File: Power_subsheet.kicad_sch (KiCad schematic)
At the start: 26 parts, among them U5 LM1117MP-ADJ, U7 TPS54331-Q1

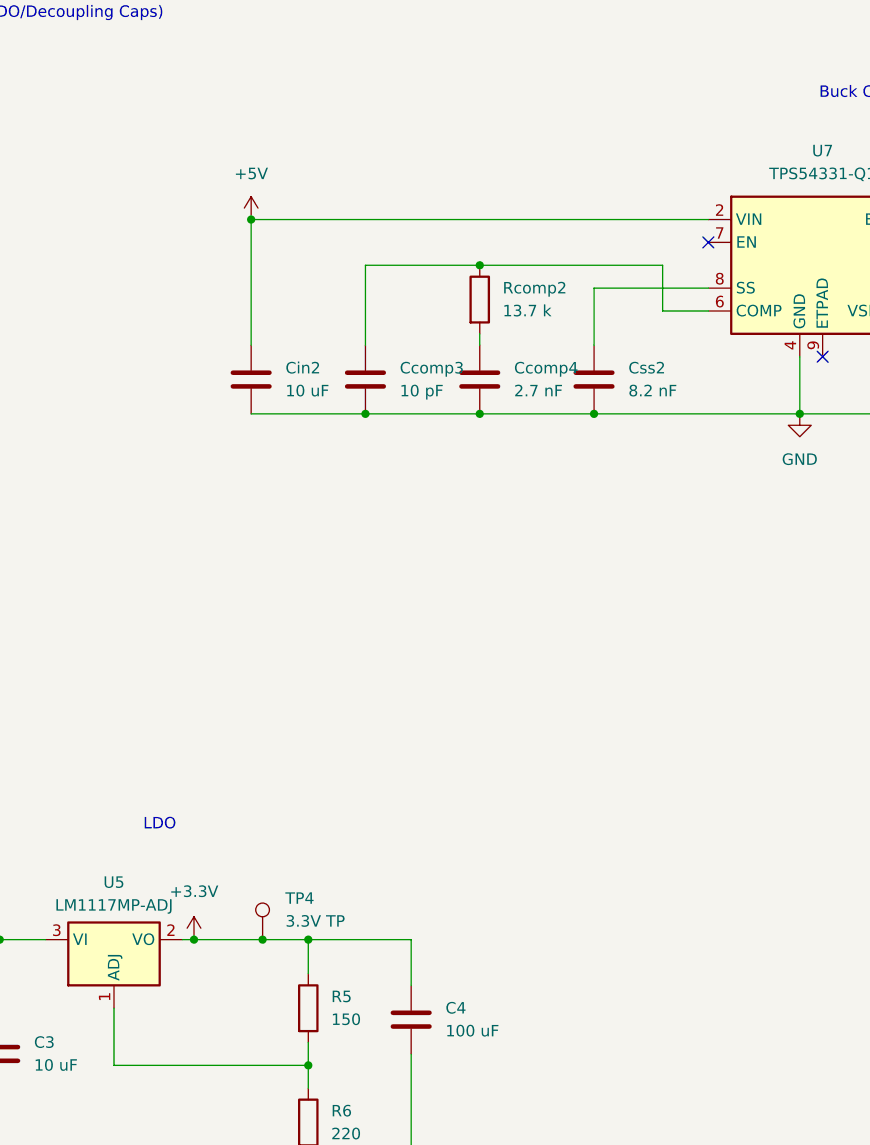
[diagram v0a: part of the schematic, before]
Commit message: remove un-needed program header circuitry, add debug LEDs, add USB ESD, add shcotty for LM117
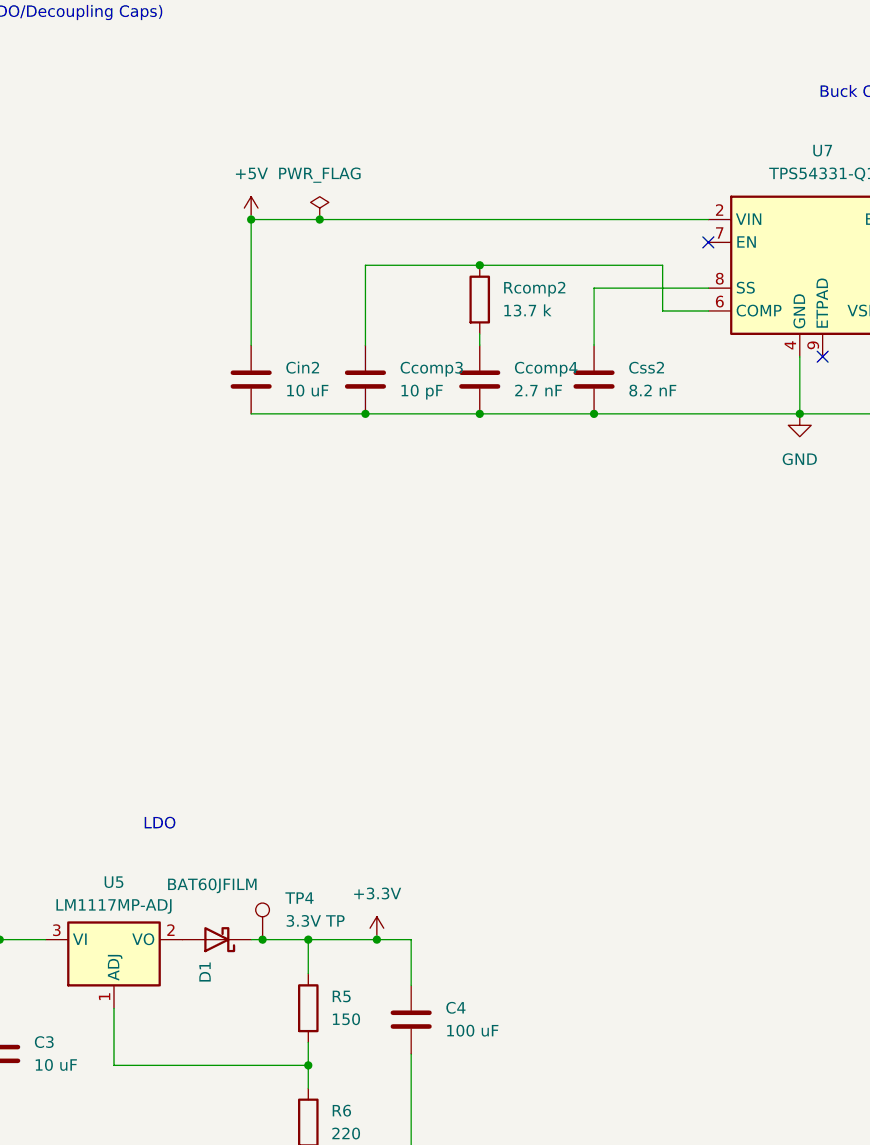
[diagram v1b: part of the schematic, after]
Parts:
- added D1: BAT60JFILM, Diode_SMD:D_0805_2012Metric_Pad1.15x1.40mm_HandSolder, symbol Device:D_Schottky
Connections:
- net +3.3V: now also D1.1 (K); no longer U5.2 (VO)
- new net: D1.2 (A), U5.2 (VO)

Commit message: more cap changes
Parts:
- added C6: 4.7 uF, Capacitor_SMD:C_0805_2012Metric_Pad1.18x1.45mm_HandSolder, symbol Device:C
- added C7: 1 uF, Capacitor_SMD:C_0805_2012Metric_Pad1.18x1.45mm_HandSolder, symbol Device:C
- C21: value 10 uF -> 10 nF
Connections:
- net +3.3V: now also C6.1, C7.1
- net GND: now also C6.2, C7.2
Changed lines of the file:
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@@
 	)
 	(junction
+		(at 242.57 133.35)
+		(diameter 0)
+		(color 0 0 0 0)
+	)
+	(junction
 		(at 220.98 140.97)
 		(diameter 0)
@@
 	)
 	(junction
+		(at 255.27 133.35)
+		(diameter 0)
+		(color 0 0 0 0)
+	)
+	(junction
 		(at 134.62 67.31)
 		(diameter 0)
@@
 	)
 	(junction
+		(at 255.27 140.97)
+		(diameter 0)
+		(color 0 0 0 0)
+	)
+	(junction
 		(at 210.82 140.97)
 		(diameter 0)
@@
 	(wire
 		(pts
+			(xy 242.57 133.35) (xy 255.27 133.35)
+		)
+		(stroke
+			(width 0)
+			(type default)
+		)
+	)
+	(wire
+		(pts
 			(xy 99.06 58.42) (xy 99.06 59.69)
 		)
@@
 	(wire
 		(pts
+			(xy 255.27 133.35) (xy 267.97 133.35)
+		)
+		(stroke
+			(width 0)
+			(type default)
+		)
+	)
+	(wire
+		(pts
 			(xy 99.06 50.8) (xy 119.38 50.8)
 		)
@@
 	(wire
 		(pts
+			(xy 242.57 140.97) (xy 255.27 140.97)
+		)
+		(stroke
+			(width 0)
+			(type default)
+		)
+	)
+	(wire
+		(pts
 			(xy 80.01 137.16) (xy 80.01 139.7)
 		)
@@
 	(wire
 		(pts
+			(xy 255.27 140.97) (xy 267.97 140.97)
+		)
+		(stroke
+			(width 0)
+			(type default)
+		)
+	)
+	(wire
+		(pts
 			(xy 220.98 133.35) (xy 231.14 133.35)
 		)
@@
 			)
 		)
-		(property "Value" "10 uF"
+		(property "Value" "10 nF"
 			(at 246.38 138.4299 0)
 			(effects
@@
 	)
 	(symbol
+		(lib_id "Device:C")
+		(at 267.97 137.16 0)
+		(unit 1)
+		(exclude_from_sim no)
+		(in_bom yes)
+		(on_board yes)
+		(dnp no)
+		(fields_autoplaced yes)
+		(property "Reference" "C7"
+			(at 271.78 135.8899 0)
+			(effects
+				(font
+					(size 1.27 1.27)
+				)
+				(justify left)
+			)
+		)
+		(property "Value" "1 uF"
+			(at 271.78 138.4299 0)
+			(effects
+				(font
+					(size 1.27 1.27)
+				)
+				(justify left)
+			)
+		)
+		(property "Footprint" "Capacitor_SMD:C_0805_2012Metric_Pad1.18x1.45mm_HandSolder"
+			(at 268.9352 140.97 0)
+			(effects
+				(font
+					(size 1.27 1.27)
+				)
+				(hide yes)
+			)
+		)
+		(property "Datasheet" "~"
+			(at 267.97 137.16 0)
+			(effects
+				(font
+					(size 1.27 1.27)
+				)
+				(hide yes)
+			)
+		)
+		(property "Description" "Unpolarized capacitor"
+			(at 267.97 137.16 0)
+			(effects
+				(font
+					(size 1.27 1.27)
+				)
+				(hide yes)
+			)
+		)
+		(pin "1"
+		)
+		(pin "2"
+		)
+		(instances
+			(project "PCB_Schematic"
+				(path "/a0c17764-e0d1-4df5-b871-1489cf266494/e6fb26c7-dfd6-4c6c-883e-94dceb19958a"
+					(reference "C7")
+					(unit 1)
+				)
+			)
+		)
+	)
+	(symbol
 		(lib_id "Device:R")
 		(at 99.06 54.61 0)
@@
 					(unit 1)
 				)
+			)
+		)
+	)
+	(symbol
+		(lib_id "Device:C")
+		(at 255.27 137.16 0)
+		(unit 1)
+		(exclude_from_sim no)
+		(in_bom yes)
+		(on_board yes)
+		(dnp no)
+		(fields_autoplaced yes)
+		(property "Reference" "C6"
+			(at 259.08 135.8899 0)
+			(effects
+				(font
+					(size 1.27 1.27)
+				)
+				(justify left)
+			)
+		)
+		(property "Value" "4.7 uF"
+			(at 259.08 138.4299 0)
+			(effects
+				(font
+					(size 1.27 1.27)
+				)
+				(justify left)
+			)
+		)
+		(property "Footprint" "Capacitor_SMD:C_0805_2012Metric_Pad1.18x1.45mm_HandSolder"
+			(at 256.2352 140.97 0)
+			(effects
+				(font
+					(size 1.27 1.27)
+				)
+				(hide yes)
+			)
+		)
+		(property "Datasheet" "~"
+			(at 255.27 137.16 0)
+			(effects
+				(font
+					(size 1.27 1.27)
+				)
+				(hide yes)
+			)
+		)
+		(property "Description" "Unpolarized capacitor"
+			(at 255.27 137.16 0)
+			(effects
+				(font
+					(size 1.27 1.27)
+				)
+				(hide yes)
+			)
+		)
+		(pin "1"
+		)
+		(pin "2"
+		)
+		(instances
+			(project "PCB_Schematic"
+				(path "/a0c17764-e0d1-4df5-b871-1489cf266494/e6fb26c7-dfd6-4c6c-883e-94dceb19958a"
+					(reference "C6")
+					(unit 1)
+				)

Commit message: starter PCB
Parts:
- C4: renamed from C3; footprint (none) -> Capacitor_SMD:C_0805_2012Metric_Pad1.18x1.45mm_HandSolder
- C5: renamed from C4; footprint (none) -> Capacitor_SMD:C_0805_2012Metric_Pad1.18x1.45mm_HandSolder
- renumbered C20 to C10, C21 to C11, C6 to C12, C7 to C13, C5 to C6, C17 to C7, C18 to C8, C19 to C9, Cboot2 to Cboot1, Ccomp3 to Ccomp1, Ccomp4 to Ccomp2, Cin2 to Cin1, Cout2 to Cout1, Css2 to Css1, D1 to D11, D2 to D12, D3 to D13, L2 to L1, R5 to R12, R6 to R13, R16 to R14, Rcomp2 to Rcomp1, Rfbb2 to Rfbb1, Rfbt2 to Rfbt1, TP4 to TP1, U5 to U3, U7 to U4

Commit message: more
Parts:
- removed U4: TPS54331-Q1, Library:Project_TPS, symbol Regulator_Switching:TPS54336ADDA
- added C16: .1 uF, Capacitor_SMD:C_0805_2012Metric_Pad1.18x1.45mm_HandSolder, symbol Device:C
- added U4: TPS54331QDRQ1, Library:Project_TPS, symbol New_Library:TPS54331QDRQ1
- U3: footprint Library:Project_LM1117 -> Package_TO_SOT_SMD:SOT-23-3
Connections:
- net +3.3V: now also C16.1
- net +5V: now also U4.2 (VIN)
- net GND: now also C16.2, U4.7 (GND)
- net at Cboot1.1: now also D12.1 (K), L1.1, U4.8 (PH)
- net at Rfbb1.1, Rfbt1.2: now also U4.5 (VSENSE)
- net at Css1.1: now also U4.4 (SS)
- net at Ccomp1.1, Rcomp1.1: now also U4.6 (COMP)
- new net: Cboot1.2, U4.1 (BOOT)
- no-connect marks 2 -> 1
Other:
- moved on the sheet: C4, C5, D11, R12, R13, TP1, U3

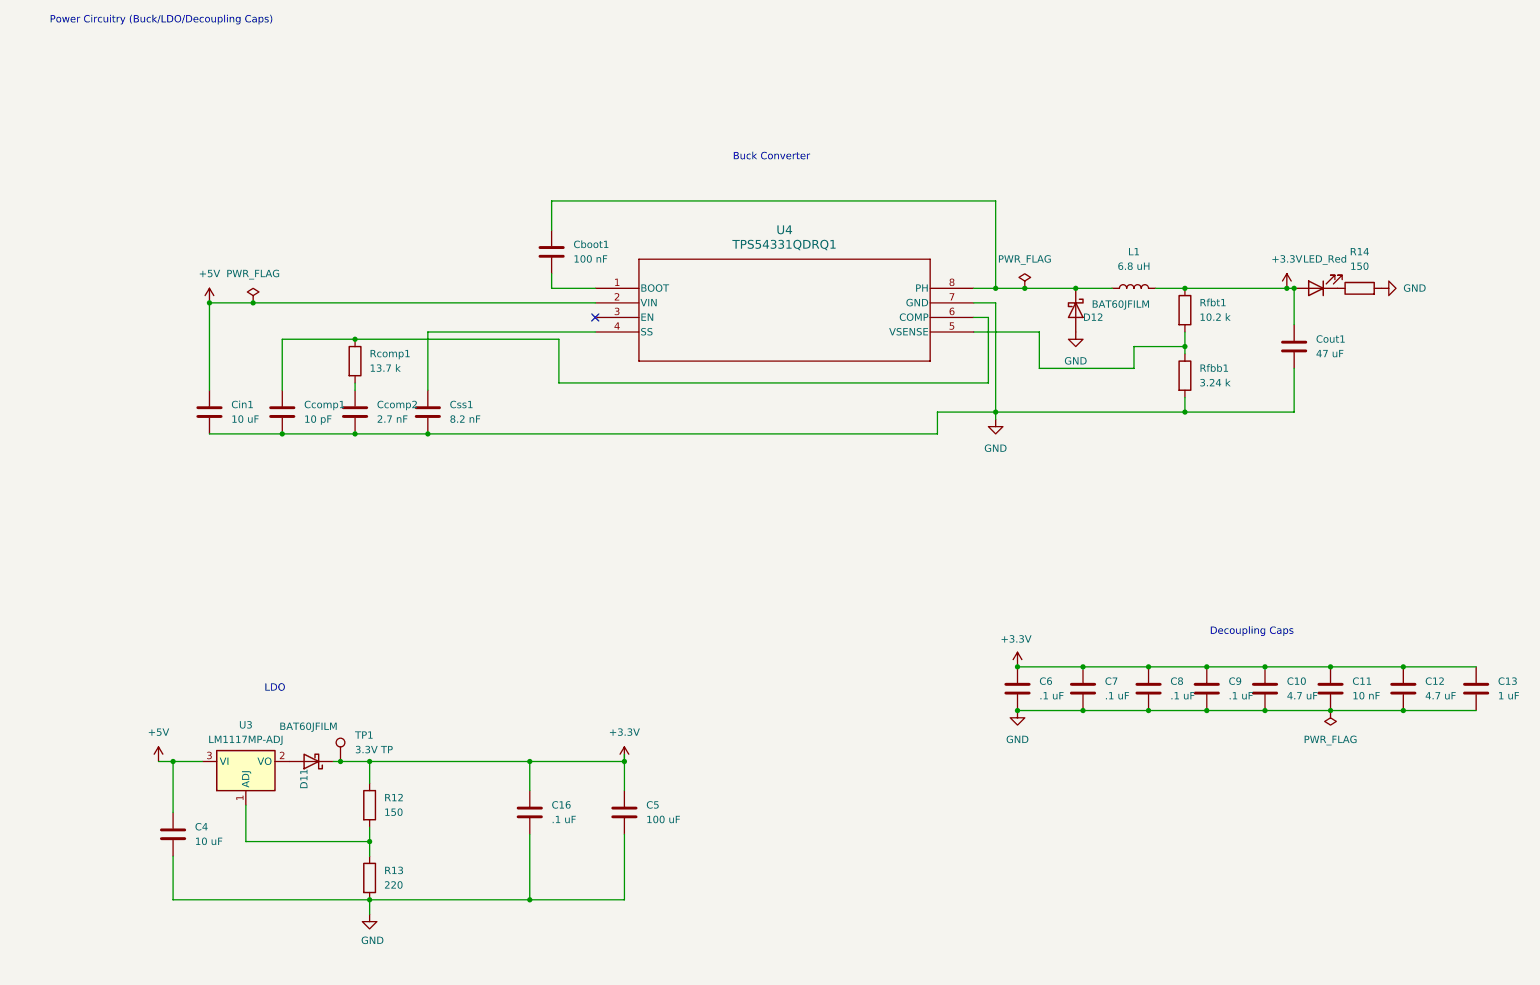
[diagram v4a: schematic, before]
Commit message: added testpoints to schematic for important sigs
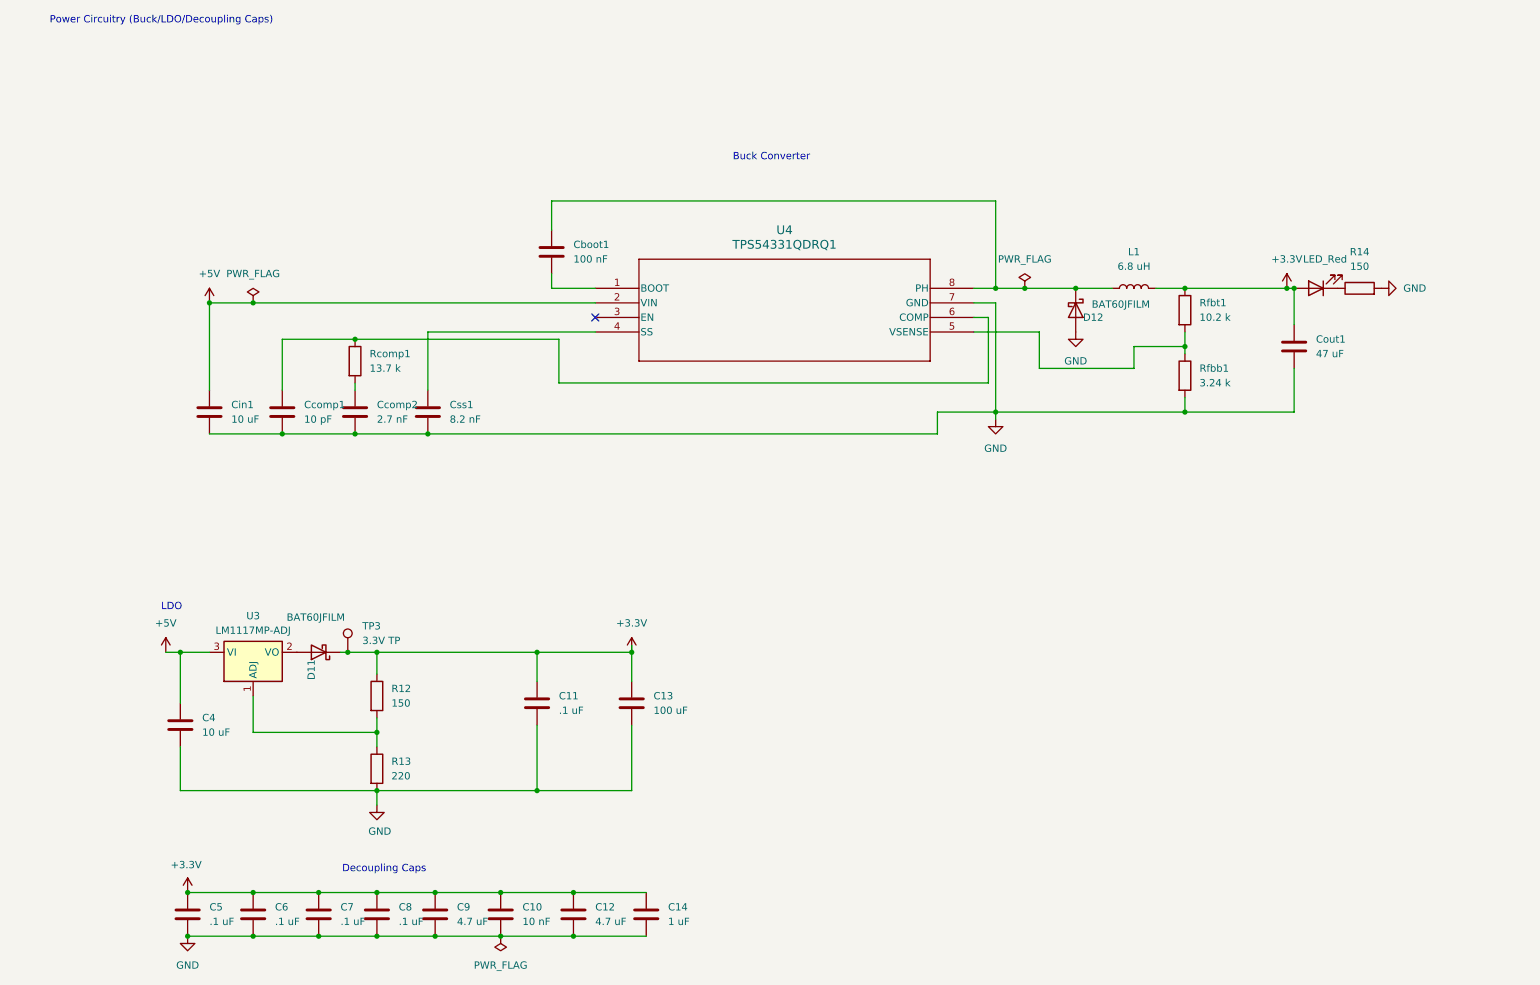
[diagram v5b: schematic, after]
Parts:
- renumbered C11 to C10, C16 to C11, C5 to C13, C13 to C14, C6 to C5, C7 to C6, C8 to C7, C9 to C8, C10 to C9, TP1 to TP3
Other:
- moved on the sheet: C10, C11, C12, C13, C14, C4, C5, C6, C7, C8, C9, D11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

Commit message: done
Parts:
- U3: footprint Package_TO_SOT_SMD:SOT-23-3 -> Library:LDO_fp
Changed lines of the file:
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@@
 			)
 		)
-		(property "Footprint" "Package_TO_SOT_SMD:SOT-23-3"
+		(property "Footprint" "Library:LDO_fp"
 			(at 54.61 130.81 0)
 			(effects

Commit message: new buck
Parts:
- Cboot1: footprint Capacitor_SMD:C_0805_2012Metric_Pad1.18x1.45mm_HandSolder -> Capacitor_SMD:C_0402_1005Metric_Pad0.74x0.62mm_HandSolder
- Cin1, Cout1: footprint Capacitor_SMD:C_0805_2012Metric_Pad1.18x1.45mm_HandSolder -> Capacitor_SMD:C_1210_3225Metric_Pad1.33x2.70mm_HandSolder
- Css1: footprint Capacitor_SMD:C_0805_2012Metric_Pad1.18x1.45mm_HandSolder -> Capacitor_SMD:C_0201_0603Metric_Pad0.64x0.40mm_HandSolder
- D12: footprint Diode_SMD:D_0805_2012Metric_Pad1.15x1.40mm_HandSolder -> Diode_SMD:D_SOD-123F
- L1: footprint Inductor_SMD:L_0805_2012Metric_Pad1.15x1.40mm_HandSolder -> Library:inductor
- Rcomp1, Rfbb1, Rfbt1: footprint Resistor_SMD:R_0805_2012Metric_Pad1.20x1.40mm_HandSolder -> Capacitor_SMD:C_0402_1005Metric_Pad0.74x0.62mm_HandSolder
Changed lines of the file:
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@@
 			)
 		)
-		(property "Footprint" "Resistor_SMD:R_0805_2012Metric_Pad1.20x1.40mm_HandSolder"
+		(property "Footprint" "Capacitor_SMD:C_0402_1005Metric_Pad0.74x0.62mm_HandSolder"
 			(at 70.612 80.01 90)
 			(effects
@@
 			)
 		)
-		(property "Footprint" "Capacitor_SMD:C_0805_2012Metric_Pad1.18x1.45mm_HandSolder"
+		(property "Footprint" "Capacitor_SMD:C_0201_0603Metric_Pad0.64x0.40mm_HandSolder"
 			(at 86.0552 92.71 0)
 			(effects
@@
 			)
 		)
-		(property "Footprint" "Resistor_SMD:R_0805_2012Metric_Pad1.20x1.40mm_HandSolder"
+		(property "Footprint" "Capacitor_SMD:C_0402_1005Metric_Pad0.74x0.62mm_HandSolder"
 			(at 215.392 82.55 90)
 			(effects
@@
 			)
 		)
-		(property "Footprint" "Capacitor_SMD:C_0805_2012Metric_Pad1.18x1.45mm_HandSolder"
+		(property "Footprint" "Capacitor_SMD:C_1210_3225Metric_Pad1.33x2.70mm_HandSolder"
 			(at 47.9552 92.71 0)
 			(effects
@@
 			)
 		)
-		(property "Footprint" "Inductor_SMD:L_0805_2012Metric_Pad1.15x1.40mm_HandSolder"
+		(property "Footprint" "Library:inductor"
 			(at 208.28 67.31 0)
 			(effects
@@
 			)
 		)
-		(property "Footprint" "Resistor_SMD:R_0805_2012Metric_Pad1.20x1.40mm_HandSolder"
+		(property "Footprint" "Capacitor_SMD:C_0402_1005Metric_Pad0.74x0.62mm_HandSolder"
 			(at 215.392 71.12 90)
 			(effects
@@
 			)
 		)
-		(property "Footprint" "Diode_SMD:D_0805_2012Metric_Pad1.15x1.40mm_HandSolder"
+		(property "Footprint" "Diode_SMD:D_SOD-123F"
 			(at 198.12 71.12 0)
 			(effects
@@
 			)
 		)
-		(property "Footprint" "Capacitor_SMD:C_0805_2012Metric_Pad1.18x1.45mm_HandSolder"
+		(property "Footprint" "Capacitor_SMD:C_1210_3225Metric_Pad1.33x2.70mm_HandSolder"
 			(at 237.1852 81.28 0)
 			(effects
@@
 			)
 		)
-		(property "Footprint" "Capacitor_SMD:C_0805_2012Metric_Pad1.18x1.45mm_HandSolder"
+		(property "Footprint" "Capacitor_SMD:C_0402_1005Metric_Pad0.74x0.62mm_HandSolder"
 			(at 107.6452 64.77 0)
 			(effects

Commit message: updated stuff
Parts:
- Css1: footprint Capacitor_SMD:C_0201_0603Metric_Pad0.64x0.40mm_HandSolder -> Capacitor_SMD:C_0201_0603Metric
- U3: footprint Library:LDO_fp -> Package_TO_SOT_SMD:SOT-223
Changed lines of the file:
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@@
 			)
 		)
-		(property "Footprint" "Capacitor_SMD:C_0201_0603Metric_Pad0.64x0.40mm_HandSolder"
+		(property "Footprint" "Capacitor_SMD:C_0201_0603Metric"
 			(at 86.0552 92.71 0)
 			(effects
@@
 			)
 		)
-		(property "Footprint" "Library:LDO_fp"
+		(property "Footprint" "Package_TO_SOT_SMD:SOT-223"
 			(at 54.61 130.81 0)
 			(effects
